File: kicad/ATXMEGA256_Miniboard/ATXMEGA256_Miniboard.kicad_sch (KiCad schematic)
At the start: 25 parts, among them J2 10118192-0001LF, J3 2x5 IDC Socket, J5 2x3 Goldpin Header, SW1 RESET, U1 ATXMEGA256A3B-AU, Y2 16 MHz, Y3 32.768 kHz

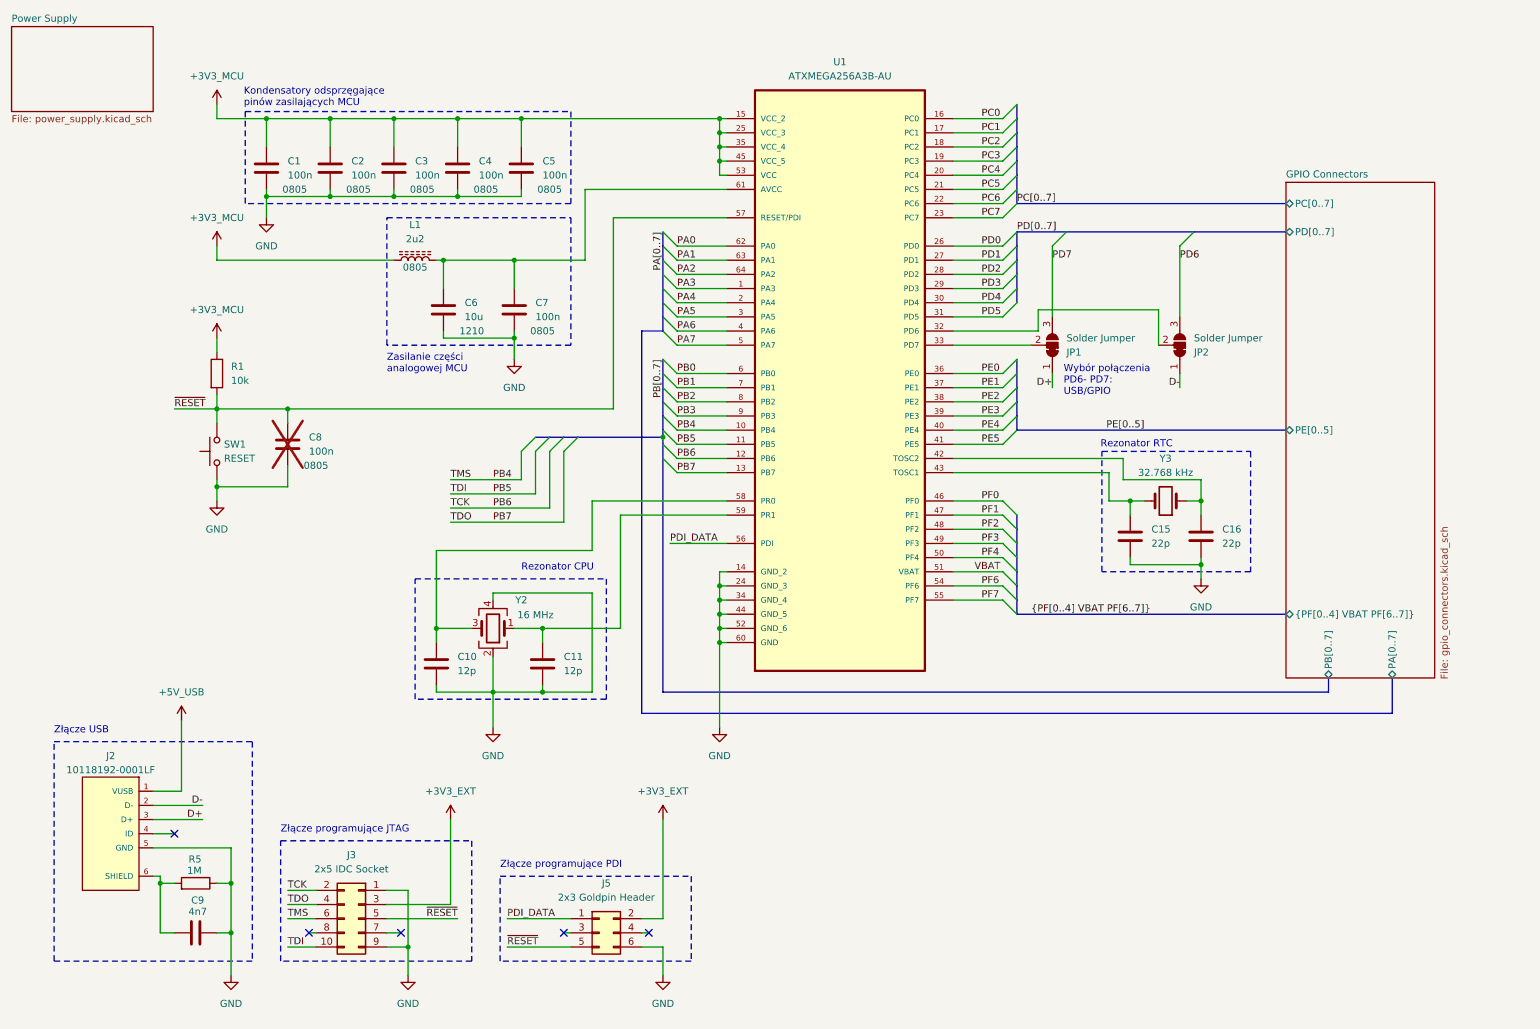
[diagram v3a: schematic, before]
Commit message: Zmiana zlacza PDI, dodany makefile i struktura plikow
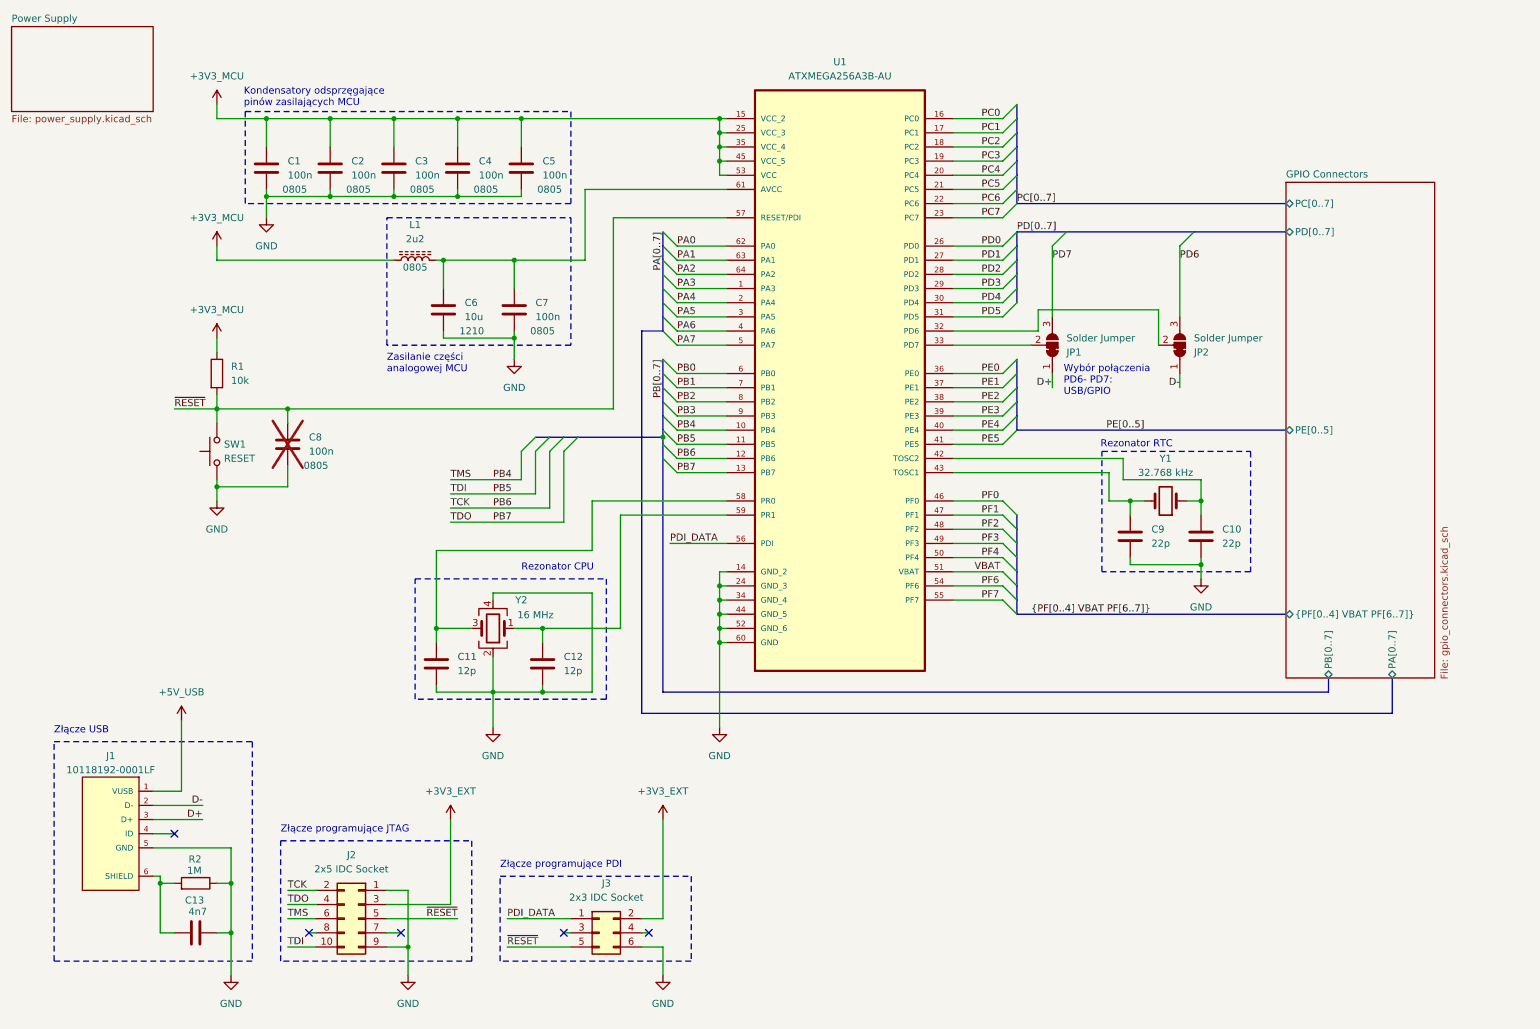
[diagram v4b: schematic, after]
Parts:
- J3: renamed from J5; value 2x3 Goldpin Header -> 2x3 IDC Socket; footprint Connector_PinHeader_2.54mm:PinHeader_2x03_P2.54mm_Vertical_SMD -> Connector_IDC:IDC-Header_2x03_P2.54mm_Vertical; Manufacturer CONNFLY -> AMPHENOL COMMUNICATIONS SOLUTIONS; Part Number DS1021-2*3SF11-B -> T821106A1S100CEU
- renumbered C16 to C10, C10 to C11, C11 to C12, C9 to C13, C15 to C9, J2 to J1, J3 to J2, R5 to R2, Y3 to Y1
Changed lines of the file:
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@@
 		(dnp no)
 		(fields_autoplaced yes)
-		(property "Reference" "Y3"
+		(property "Reference" "Y1"
 			(at 223.52 95.25 0)
 			(effects
@@
 			(project ""
 				(path "/ef1e5883-c6cf-4bad-8eaa-8ec9109f9d71"
-					(reference "Y3")
+					(reference "Y1")
 					(unit 1)
 				)
@@
 		(dnp no)
 		(fields_autoplaced yes)
-		(property "Reference" "#PWR012"
+		(property "Reference" "#PWR014"
 			(at 87.63 194.31 0)
 			(effects
@@
 			(project "ATXMEGA256_Miniboard"
 				(path "/ef1e5883-c6cf-4bad-8eaa-8ec9109f9d71"
-					(reference "#PWR012")
+					(reference "#PWR014")
 					(unit 1)
 				)
@@
 		(on_board yes)
 		(dnp no)
-		(property "Reference" "#PWR08"
+		(property "Reference" "#PWR09"
 			(at 102.87 149.86 0)
 			(effects
@@
 			(project "ATXMEGA256_Miniboard"
 				(path "/ef1e5883-c6cf-4bad-8eaa-8ec9109f9d71"
-					(reference "#PWR08")
+					(reference "#PWR09")
 					(unit 1)
 				)
@@
 		(on_board yes)
 		(dnp no)
-		(property "Reference" "C9"
+		(property "Reference" "C13"
 			(at 51.054 174.498 90)
 			(effects
@@
 			(project "ATXMEGA256_Miniboard"
 				(path "/ef1e5883-c6cf-4bad-8eaa-8ec9109f9d71"
-					(reference "C9")
+					(reference "C13")
 					(unit 1)
 				)
@@
 		(on_board yes)
 		(dnp no)
-		(property "Reference" "C15"
+		(property "Reference" "C9"
 			(at 220.98 107.95 0)
 			(effects
@@
 			(project "ATXMEGA256_Miniboard"
 				(path "/ef1e5883-c6cf-4bad-8eaa-8ec9109f9d71"
-					(reference "C15")
+					(reference "C9")
 					(unit 1)
 				)
@@
 		(dnp no)
 		(fields_autoplaced yes)
-		(property "Reference" "#PWR036"
+		(property "Reference" "#PWR01"
 			(at 53.34 35.56 0)
 			(effects
@@
 			(project "ATXMEGA256_Miniboard"
 				(path "/ef1e5883-c6cf-4bad-8eaa-8ec9109f9d71"
-					(reference "#PWR036")
+					(reference "#PWR01")
 					(unit 1)
 				)
@@
 		(dnp no)
 		(fields_autoplaced yes)
-		(property "Reference" "#PWR043"
+		(property "Reference" "#PWR012"
 			(at 133.35 163.83 0)
 			(effects
@@
 			(project "ATXMEGA256_Miniboard"
 				(path "/ef1e5883-c6cf-4bad-8eaa-8ec9109f9d71"
-					(reference "#PWR043")
+					(reference "#PWR012")
 					(unit 1)
 				)
@@
 		(on_board yes)
 		(dnp no)
-		(property "Reference" "C16"
+		(property "Reference" "C10"
 			(at 233.68 107.95 0)
 			(effects
@@
 			(project "ATXMEGA256_Miniboard"
 				(path "/ef1e5883-c6cf-4bad-8eaa-8ec9109f9d71"
-					(reference "C16")
+					(reference "C10")
 					(unit 1)
 				)
@@
 		(dnp no)
 		(fields_autoplaced yes)
-		(property "Reference" "J5"
+		(property "Reference" "J3"
 			(at 123.19 171.45 0)
 			(effects
@@
 			)
 		)
-		(property "Value" "2x3 Goldpin Header"
+		(property "Value" "2x3 IDC Socket"
 			(at 123.19 173.99 0)
 			(effects
@@
 			)
 		)
-		(property "Footprint" "Connector_PinHeader_2.54mm:PinHeader_2x03_P2.54mm_Vertical_SMD"
+		(property "Footprint" "Connector_IDC:IDC-Header_2x03_P2.54mm_Vertical"
 			(at 121.92 180.34 0)
 			(effects
@@
 			)
 		)
-		(property "Part Number" "DS1021-2*3SF11-B"
+		(property "Part Number" "T821106A1S100CEU"
 			(at 121.92 180.34 0)
 			(effects
@@
 			)
 		)
-		(property "Manufacturer" "CONNFLY"
+		(property "Manufacturer" "AMPHENOL COMMUNICATIONS SOLUTIONS"
 			(at 121.92 180.34 0)
 			(effects
@@
 			(project "ATXMEGA256_Miniboard"
 				(path "/ef1e5883-c6cf-4bad-8eaa-8ec9109f9d71"
-					(reference "J5")
+					(reference "J3")
 					(unit 1)
 				)
@@
 		(on_board yes)
 		(dnp no)
-		(property "Reference" "C11"
+		(property "Reference" "C12"
 			(at 115.57 130.81 0)
 			(effects
@@
 			(project "ATXMEGA256_Miniboard"
 				(path "/ef1e5883-c6cf-4bad-8eaa-8ec9109f9d71"
-					(reference "C11")
+					(reference "C12")
 					(unit 1)
 				)
@@
 		(on_board yes)
 		(dnp no)
-		(property "Reference" "R5"
+		(property "Reference" "R2"
 			(at 48.26 167.132 90)
 			(effects
@@
 			(project "ATXMEGA256_Miniboard"
 				(path "/ef1e5883-c6cf-4bad-8eaa-8ec9109f9d71"
-					(reference "R5")
+					(reference "R2")
 					(unit 1)
 				)
@@
 		(dnp no)
 		(fields_autoplaced yes)
-		(property "Reference" "#PWR037"
+		(property "Reference" "#PWR03"
 			(at 53.34 60.96 0)
 			(effects
@@
 			(project "ATXMEGA256_Miniboard"
 				(path "/ef1e5883-c6cf-4bad-8eaa-8ec9109f9d71"
-					(reference "#PWR037")
+					(reference "#PWR03")
 					(unit 1)
 				)
@@
 		(on_board yes)
 		(dnp no)
-		(property "Reference" "C10"
+		(property "Reference" "C11"
 			(at 96.52 130.81 0)
 			(effects
@@
 			(project "ATXMEGA256_Miniboard"
 				(path "/ef1e5883-c6cf-4bad-8eaa-8ec9109f9d71"
-					(reference "C10")
+					(reference "C11")
 					(unit 1)
 				)
@@
 		(dnp no)
 		(fields_autoplaced yes)
-		(property "Reference" "#PWR04"
+		(property "Reference" "#PWR08"
 			(at 46.99 146.05 0)
 			(effects
@@
 			(project "ATXMEGA256_Miniboard"
 				(path "/ef1e5883-c6cf-4bad-8eaa-8ec9109f9d71"
-					(reference "#PWR04")
+					(reference "#PWR08")
 					(unit 1)
 				)
@@
 		(dnp no)
 		(fields_autoplaced yes)
-		(property "Reference" "J3"
+		(property "Reference" "J2"
 			(at 77.47 166.37 0)
 			(effects
@@
 			(project "ATXMEGA256_Miniboard"
 				(path "/ef1e5883-c6cf-4bad-8eaa-8ec9109f9d71"
-					(reference "J3")
+					(reference "J2")
 					(unit 1)
 				)
@@
 		(dnp no)
 		(fields_autoplaced yes)
-		(property "Reference" "#PWR042"
+		(property "Reference" "#PWR011"
 			(at 95.25 163.83 0)
 			(effects
@@
 			(project "ATXMEGA256_Miniboard"
 				(path "/ef1e5883-c6cf-4bad-8eaa-8ec9109f9d71"
-					(reference "#PWR042")
+					(reference "#PWR011")
 					(unit 1)
 				)
@@
 		(dnp no)
 		(fields_autoplaced yes)
-		(property "Reference" "#PWR09"
+		(property "Reference" "#PWR010"
 			(at 143.51 149.86 0)
 			(effects
@@
 			(project "ATXMEGA256_Miniboard"
 				(path "/ef1e5883-c6cf-4bad-8eaa-8ec9109f9d71"
-					(reference "#PWR09")
+					(reference "#PWR010")
 					(unit 1)
 				)
@@
 		(dnp no)
 		(fields_autoplaced yes)
-		(property "Reference" "#PWR038"
+		(property "Reference" "#PWR04"
 			(at 53.34 77.47 0)
 			(effects
@@
 			(project "ATXMEGA256_Miniboard"
 				(path "/ef1e5883-c6cf-4bad-8eaa-8ec9109f9d71"
-					(reference "#PWR038")
+					(reference "#PWR04")
 					(unit 1)
 				)
@@
 		(on_board yes)
 		(dnp no)
-		(property "Reference" "#PWR010"
+		(property "Reference" "#PWR07"
 			(at 229.87 123.19 0)
 			(effects
@@
 			(project "ATXMEGA256_Miniboard"
 				(path "/ef1e5883-c6cf-4bad-8eaa-8ec9109f9d71"
-					(reference "#PWR010")
+					(reference "#PWR07")
 					(unit 1)
 				)
@@
 		(dnp no)
 		(fields_autoplaced yes)
-		(property "Reference" "#PWR05"
+		(property "Reference" "#PWR06"
 			(at 53.34 109.22 0)
 			(effects
@@
 			(project "ATXMEGA256_Miniboard"
 				(path "/ef1e5883-c6cf-4bad-8eaa-8ec9109f9d71"
-					(reference "#PWR05")
+					(reference "#PWR06")
 					(unit 1)
 				)
@@
 		(on_board yes)
 		(dnp no)
-		(property "Reference" "#PWR03"
+		(property "Reference" "#PWR05"
 			(at 106.68 83.82 0)
 			(effects
@@
 			(project "ATXMEGA256_Miniboard"
 				(path "/ef1e5883-c6cf-4bad-8eaa-8ec9109f9d71"
-					(reference "#PWR03")
+					(reference "#PWR05")
 					(unit 1)
 				)
@@
 		(dnp no)
 		(fields_autoplaced yes)
-		(property "Reference" "#PWR013"
+		(property "Reference" "#PWR015"
 			(at 133.35 194.31 0)
 			(effects
@@
 			(project "ATXMEGA256_Miniboard"
 				(path "/ef1e5883-c6cf-4bad-8eaa-8ec9109f9d71"
-					(reference "#PWR013")
+					(reference "#PWR015")
 					(unit 1)
 				)
@@
 		(on_board yes)
 		(dnp no)
-		(property "Reference" "J2"
+		(property "Reference" "J1"
 			(at 34.29 148.59 0)
 			(effects
@@
 			(project "ATXMEGA256_Miniboard"
 				(path "/ef1e5883-c6cf-4bad-8eaa-8ec9109f9d71"
-					(reference "J2")
+					(reference "J1")
 					(unit 1)
 				)
@@
 		(dnp no)
 		(fields_autoplaced yes)
-		(property "Reference" "#PWR07"
+		(property "Reference" "#PWR013"
 			(at 55.88 194.31 0)
 			(effects
@@
 			(project "ATXMEGA256_Miniboard"
 				(path "/ef1e5883-c6cf-4bad-8eaa-8ec9109f9d71"
-					(reference "#PWR07")
+					(reference "#PWR013")
 					(unit 1)
 				)

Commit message: layout komponentów
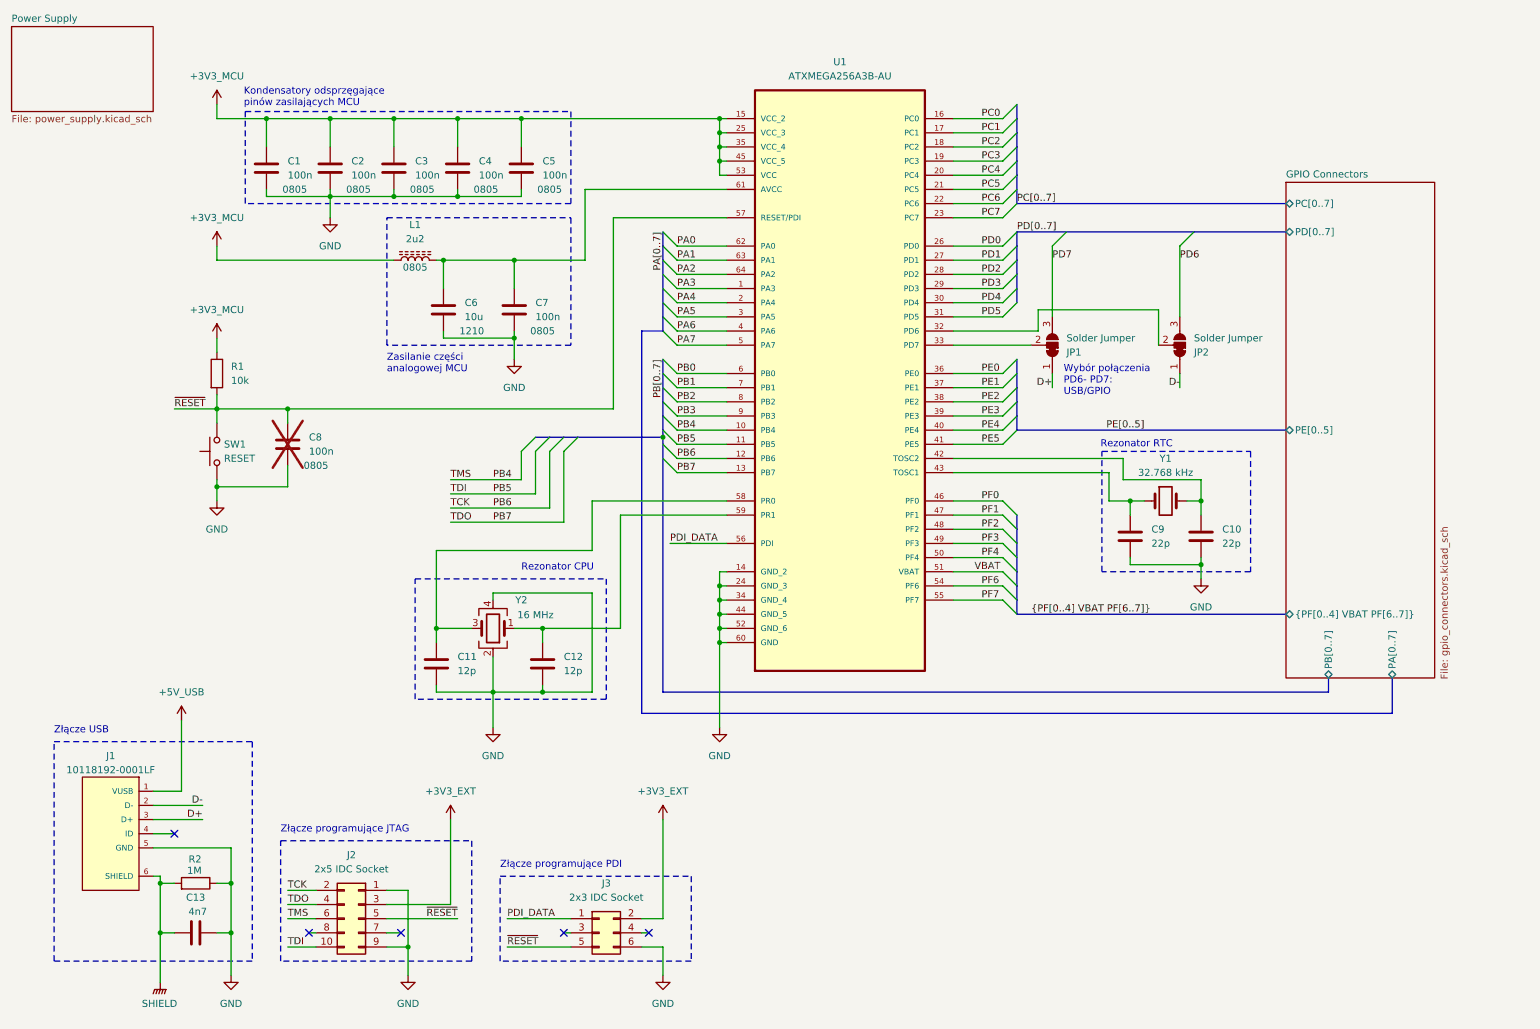
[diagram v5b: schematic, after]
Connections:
- net at C10.2, U1.42 (TOSC2): now also Y1.2; no longer Y1.1
- net at C9.2, U1.43 (TOSC1): now also Y1.1; no longer Y1.2
- net SHIELD: now reaches C13.2, J1.6 (SHIELD), R2.2
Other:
- moved on the sheet: Y1
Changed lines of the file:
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@@
 	)
 	(junction
-		(at 62.23 48.26)
-		(diameter 0)
-		(color 0 0 0 0)
-	)
-	(junction
 		(at 143.51 125.73)
 		(diameter 0)
@@
 	)
 	(junction
+		(at 43.18 180.34)
+		(diameter 0)
+		(color 0 0 0 0)
+	)
+	(junction
 		(at 107.95 34.29)
 		(diameter 0)
@@
 		)
 	)
-	(wire
-		(pts
-			(xy 92.71 125.73) (xy 99.06 125.73)
-		)
-		(stroke
-			(width 0)
-			(type default)
-		)
-	)
 	(bus
 		(pts
@@
 		)
 	)
+	(wire
+		(pts
+			(xy 43.18 180.34) (xy 43.18 189.23)
+		)
+		(stroke
+			(width 0)
+			(type default)
+		)
+	)
 	(bus
 		(pts
@@
 		)
 	)
-	(bus
+	(wire
 		(pts
-			(xy 118.11 91.44) (xy 133.35 91.44)
+			(xy 227.33 102.87) (xy 229.87 102.87)
 		)
 		(stroke
@@
 		)
 	)
-	(wire
+	(bus
 		(pts
-			(xy 229.87 114.3) (xy 229.87 116.84)
+			(xy 118.11 91.44) (xy 133.35 91.44)
 		)
 		(stroke
@@
 	(wire
 		(pts
-			(xy 62.23 46.99) (xy 62.23 48.26)
+			(xy 229.87 114.3) (xy 229.87 116.84)
 		)
 		(stroke
@@
 	(wire
 		(pts
-			(xy 185.42 102.87) (xy 194.31 102.87)
+			(xy 62.23 46.99) (xy 62.23 48.26)
 		)
 		(stroke
@@
 	(wire
 		(pts
-			(xy 135.89 92.71) (xy 144.78 92.71)
+			(xy 185.42 102.87) (xy 194.31 102.87)
 		)
 		(stroke
@@
 	(wire
 		(pts
-			(xy 229.87 102.87) (xy 227.33 102.87)
+			(xy 135.89 92.71) (xy 144.78 92.71)
 		)
 		(stroke
@@
 	(wire
 		(pts
-			(xy 219.71 102.87) (xy 217.17 102.87)
+			(xy 215.9 99.06) (xy 229.87 99.06)
 		)
 		(stroke
@@
 	(wire
 		(pts
+			(xy 217.17 102.87) (xy 219.71 102.87)
+		)
+		(stroke
+			(width 0)
+			(type default)
+		)
+	)
+	(wire
+		(pts
 			(xy 62.23 34.29) (xy 73.66 34.29)
 		)
@@
 	(wire
 		(pts
-			(xy 62.23 48.26) (xy 62.23 52.07)
+			(xy 73.66 48.26) (xy 73.66 52.07)
 		)
 		(stroke
@@
 	(wire
 		(pts
-			(xy 229.87 99.06) (xy 215.9 99.06)
-		)
-		(stroke
-			(width 0)
-			(type default)
-		)
-	)
-	(wire
-		(pts
 			(xy 53.34 100.33) (xy 53.34 102.87)
 		)
@@
 	(wire
 		(pts
+			(xy 92.71 125.73) (xy 99.06 125.73)
+		)
+		(stroke
+			(width 0)
+			(type default)
+		)
+	)
+	(wire
+		(pts
 			(xy 85.09 48.26) (xy 73.66 48.26)
 		)
@@
 	(symbol
 		(lib_id "Device:Crystal")
-		(at 223.52 102.87 180)
+		(at 223.52 102.87 0)
 		(unit 1)
 		(exclude_from_sim no)
@@
 	(symbol
 		(lib_id "power:GND")
-		(at 62.23 52.07 0)
+		(at 73.66 52.07 0)
 		(unit 1)
 		(exclude_from_sim no)
@@
 		(dnp no)
 		(property "Reference" "#PWR02"
-			(at 62.23 58.42 0)
+			(at 73.66 58.42 0)
 			(effects
 				(font
@@
 		)
 		(property "Value" "GND"
-			(at 62.23 57.15 0)
+			(at 73.66 57.15 0)
 			(effects
 				(font
@@
 		)
 		(property "Footprint" ""
-			(at 62.23 52.07 0)
+			(at 73.66 52.07 0)
 			(effects
 				(font
@@
 		)
 		(property "Datasheet" ""
-			(at 62.23 52.07 0)
+			(at 73.66 52.07 0)
 			(effects
 				(font
@@
 		)
 		(property "Description" ""
-			(at 62.23 52.07 0)
+			(at 73.66 52.07 0)
 			(effects
 				(font
@@
 		(dnp no)
 		(property "Reference" "C13"
-			(at 51.054 174.498 90)
+			(at 49.53 173.99 90)
 			(effects
 				(font
 					(size 1.27 1.27)
 				)
-				(justify right)
 			)
 		)
@@
 					(unit 1)
 				)
+			)
+		)
+	)
+	(symbol
+		(lib_id "power:GNDPWR")
+		(at 43.18 189.23 0)
+		(unit 1)
+		(exclude_from_sim no)
+		(in_bom yes)
+		(on_board yes)
+		(dnp no)
+		(fields_autoplaced yes)
+		(property "Reference" "#PWR016"
+			(at 43.18 194.31 0)
+			(effects
+				(font
+					(size 1.27 1.27)
+				)
+				(hide yes)
+			)
+		)
+		(property "Value" "SHIELD"
+			(at 43.053 193.04 0)
+			(effects
+				(font
+					(size 1.27 1.27)
+				)
+			)
+		)
+		(property "Footprint" ""
+			(at 43.18 190.5 0)
+			(effects
+				(font
+					(size 1.27 1.27)
+				)
+				(hide yes)
+			)
+		)
+		(property "Datasheet" ""
+			(at 43.18 190.5 0)
+			(effects
+				(font
+					(size 1.27 1.27)
+				)
+				(hide yes)
+			)
+		)
+		(property "Description" "Power symbol creates a global label with name \"GNDPWR\" , global ground"
+			(at 43.18 189.23 0)
+			(effects
+				(font
+					(size 1.27 1.27)
+				)
+				(hide yes)
+			)
+		)
+		(pin "1"
+		)
+		(instances
+			(project ""
+				(path "/ef1e5883-c6cf-4bad-8eaa-8ec9109f9d71"
+					(reference "#PWR016")
+					(unit 1)
+				)
